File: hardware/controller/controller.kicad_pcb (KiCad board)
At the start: 2 copper layers, 100 x 100 mm, 119 parts, among them J1 230V~, J2 LOAD, J3 DISPLAY, J4 PANEL, J5 TC top, J6 TC bot, J7 USB-C, J9 UART, Q1 AO3401A, Q2 BSS138, Q3 IRLML6346, Q4 IRLML6346, Q5 IRLML6346, Q6 AO3401A, Q7 IRLML6346, SW1 RESET, SW2 BOOT, U1 IRM-10-5, U10 USBLC6-2SC6, U11 USBLC6-2SC6, U12 USBLC6-2SC6, U2 AP7361C-33E, U3 ESP32-S3-WROOM-1U-N8, U4 USBLC6-2SC6, U5 MAX31856MUD+, U6 MAX31856MUD+, U7 SN74LVC74AD, U8 TPS3828-33DBV, U9 TC6501P065

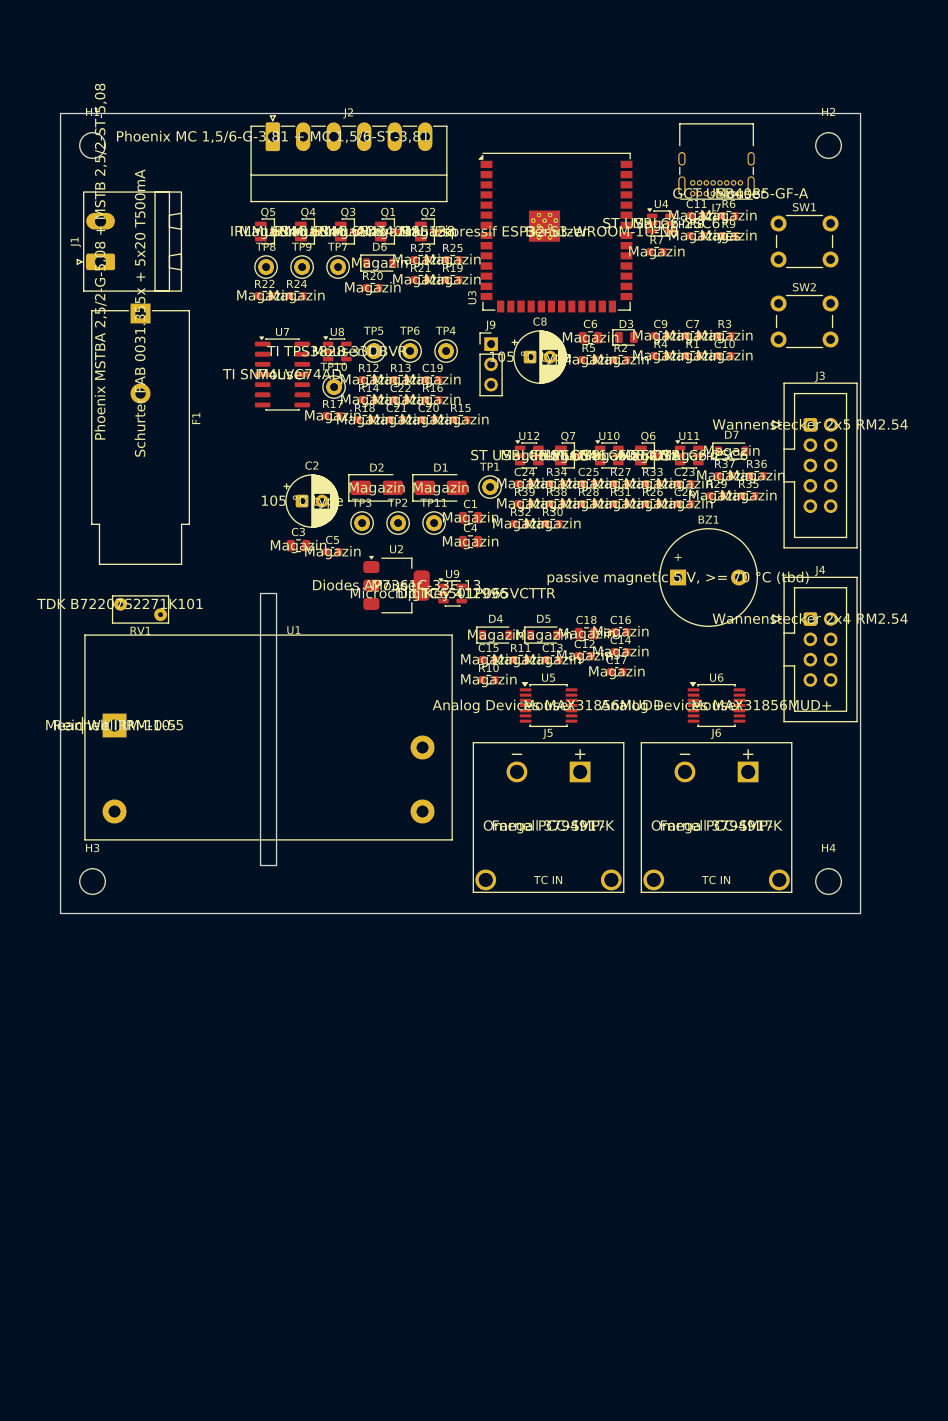
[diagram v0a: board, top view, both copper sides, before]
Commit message: fix(hardware): hide BOM fields on silkscreen, turn J1/J2 to face the board edge
- import_netlist.py sets MPN/Source/DNP fields invisible
- J1 (mains) and J2 (load) rotated 180 deg, plug side flush with the edge
- controller.kicad_pro: defaults added by KiCad 10 on first open

Co-Authored-By: Claude Opus 5.5 <noreply@anthropic.com>
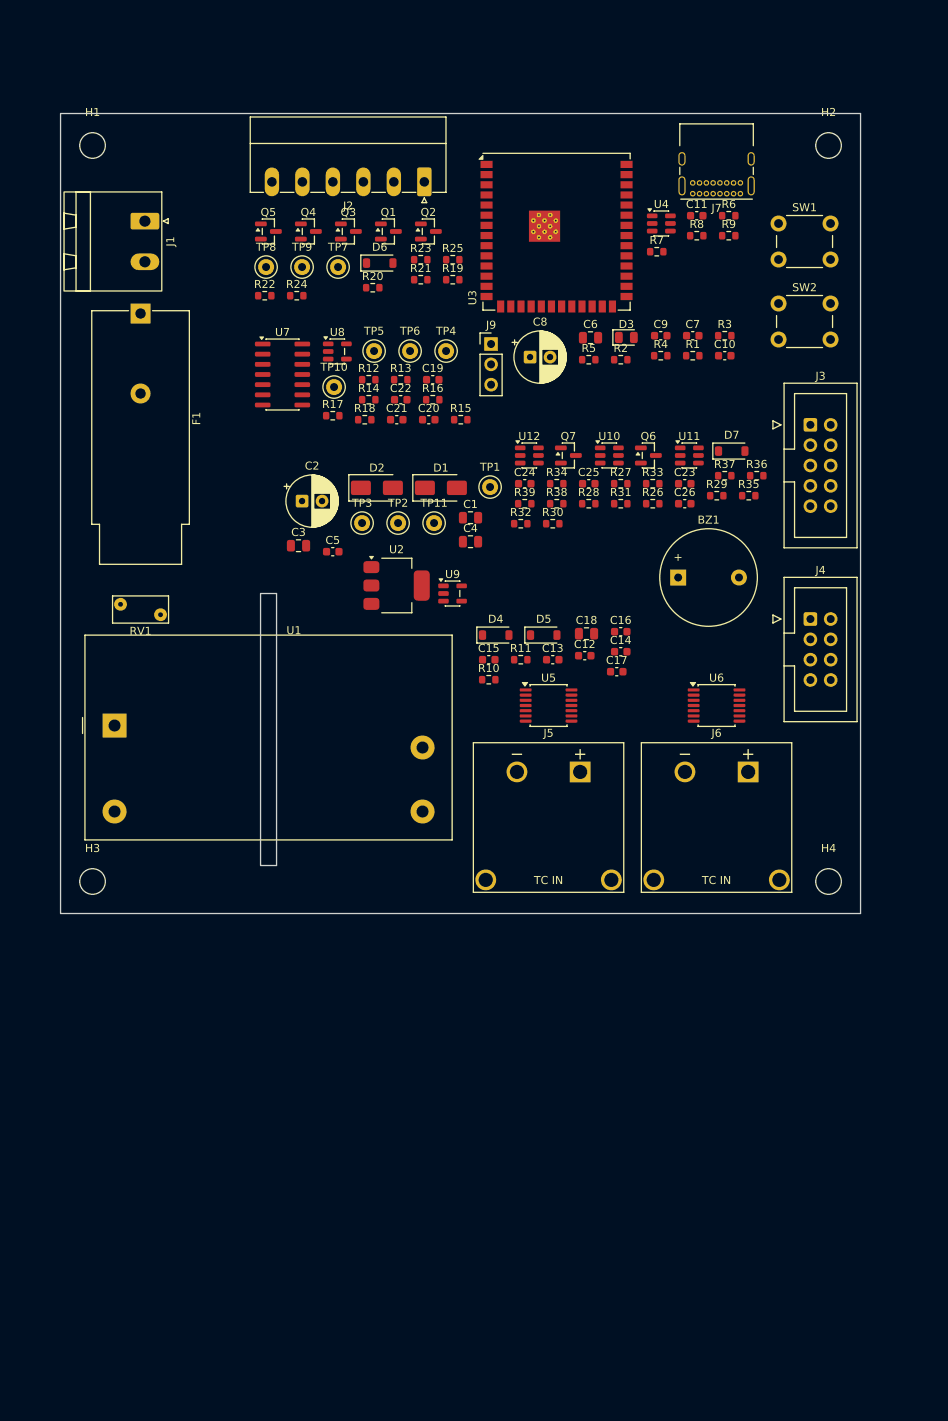
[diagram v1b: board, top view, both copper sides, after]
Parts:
- moved J2 19.8 mm to (45.5, 8.54), turned to 180 degrees
- moved J1 7.53 mm to (10.5, 13.5), turned to -90 degrees

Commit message: feat(hardware): KiCad schematic becomes the source of truth (T071, part 1)
- Schematic template generated once from SKiDL: controller (7 sheets) and encoder carrier
- Verified SKiDL netlists frozen as controller.ref.net / encoder-carrier.ref.net
- tools/check_schematic.py: compares the schematic with the reference (parts,
  connectivity, net names at the ESP32 and of net-class nets) and checks the GPIO
  assignment against board_rev_a.h; 0 errors for both boards
- Generator defects fixed: ENC_B_RAW/ENC_SW_RAW shorted by overlapping wires,
  cp1252 MPN fields, missing labels BOOT, LED_DIAG, L_FUSED (lost net class Mains)
- PCB relinked to the schematic symbols by reference, placement unchanged;
  DRC with --schematic-parity clean; mounting holes board-only
- SKiDL code moved to hardware/archive/skidl; docs and README updated

Co-Authored-By: Claude Opus 5.5 <noreply@anthropic.com>
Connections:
- net FAULT_BOT renamed Net-(D5-K)
- net FAULT_TOP renamed Net-(D4-K)
- net LED_DIAG_A renamed Net-(D3-A)
- net TFT_MOSI renamed Net-(J3-Pin_5)
- net TFT_SCK renamed Net-(J3-Pin_3)
- net USB_CC1 renamed Net-(J7-CC1)
- net USB_CC2 renamed Net-(J7-CC2)
- net USB_SHIELD renamed Net-(J7-SHIELD)
- J7 pad A8: (no net) -> unconnected-(J7-SBU1-PadA8)
- J7 pad B8: (no net) -> unconnected-(J7-SBU2-PadB8)
- U3 pad 15: (no net) -> unconnected-(U3-IO3-Pad15)
- U3 pad 16: (no net) -> unconnected-(U3-IO46-Pad16)
- U3 pad 25: (no net) -> unconnected-(U3-IO48-Pad25)
- U3 pad 26: (no net) -> unconnected-(U3-IO45-Pad26)
- U3 pad 30: (no net) -> unconnected-(U3-IO37-Pad30)
- U3 pad 31: (no net) -> unconnected-(U3-IO38-Pad31)
- U5 pad 6: (no net) -> unconnected-(U5-DNC-Pad6)
- U5 pad 7: (no net) -> unconnected-(U5-~{DRDY}-Pad7)
- U6 pad 6: (no net) -> unconnected-(U6-DNC-Pad6)
- U6 pad 7: (no net) -> unconnected-(U6-~{DRDY}-Pad7)
- U7 pad 6: (no net) -> unconnected-(U7A-~{Q}-Pad6)
- U7 pad 8: (no net) -> unconnected-(U7B-~{Q}-Pad8)
- U7 pad 9: (no net) -> unconnected-(U7B-Q-Pad9)

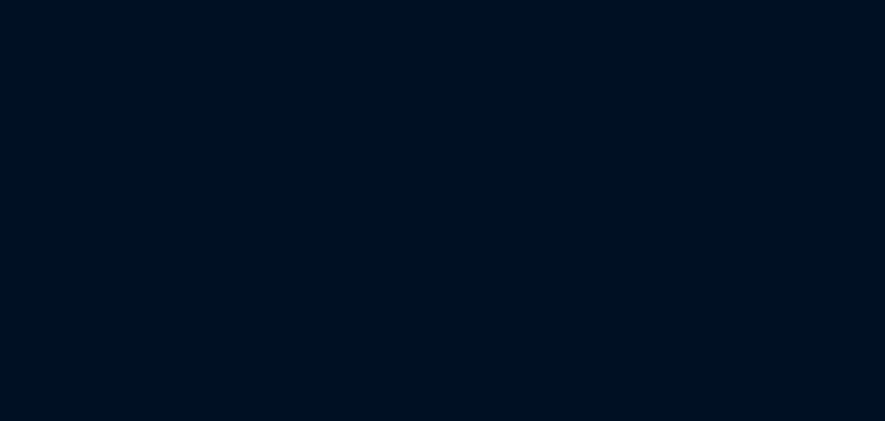
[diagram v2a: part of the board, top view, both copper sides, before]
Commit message: feat(hardware): MAX31856 input filter per datasheet, sheet cleanup in progress
- Input filter per MAX31856 "Typical Application Circuit": C14/C17 100 nF
  differential, new C27-C30 10 nF from T+/T- to GND; reference netlist re-exported
- Datasheet checks: BIAS to T- confirmed, FAULT is push-pull (diodes to CLR needed)
- check_schematic.py: sheet format check (raw newline in strings breaks KiCad)
- import_netlist.py: relinks by reference when a symbol gets a new UUID (U7 case)
- Sheets partly rearranged in KiCad by the user (connectivity unchanged, 0 errors)
- MAX31856 order number and price, docs/Component-Specs ignored

Co-Authored-By: Claude Opus 5.5 <noreply@anthropic.com>
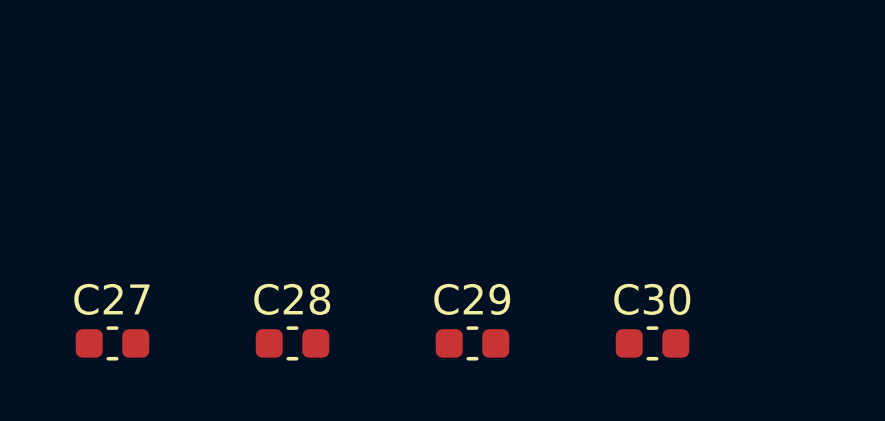
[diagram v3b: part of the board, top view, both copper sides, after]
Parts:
- added C27: 10n, Capacitor_SMD:C_0603_1608Metric, F.Cu at (0.00, 130.0)
- added C28: 10n, Capacitor_SMD:C_0603_1608Metric, F.Cu at (6.00, 130.0)
- added C29: 10n, Capacitor_SMD:C_0603_1608Metric, F.Cu at (12.0, 130.0)
- added C30: 10n, Capacitor_SMD:C_0603_1608Metric, F.Cu at (18.0, 130.0)
- C14, C17: value 10n -> 100n

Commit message: refactor(hardware): merge the 7 controller sheets into 2 (T071)
"Leistung und Sicherheit" (A3: Netzteil, Sicherheit, Last) and
"Steuerung und Messung" (A2: MCU, USB, Thermoelemente, Bedienung).
Contents are only moved, not rewired; each former sheet gets a labelled
frame. check_schematic: 119 parts, 69 nets, 0 errors; ERC unchanged.
PCB relinked by reference, placement unchanged, parity DRC clean.

Co-Authored-By: Claude Opus 5.5 <noreply@anthropic.com>
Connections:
- net ENC_A_RAW renamed /Steuerung und Messung/ENC_A_RAW
- net ENC_B_RAW renamed /Steuerung und Messung/ENC_B_RAW
- net ENC_SW_RAW renamed /Steuerung und Messung/ENC_SW_RAW
- net STOP_NO_RAW renamed /Steuerung und Messung/STOP_NO_RAW
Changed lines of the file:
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@@
 			(layers "F.Cu" "F.Mask" "F.Paste")
 			(roundrect_rratio 0.25)
-			(net "STOP_NO_RAW")
+			(net "/Steuerung und Messung/STOP_NO_RAW")
 		)
 		(pad "2" smd roundrect
@@
 			(layers "F.Cu" "F.Mask" "F.Paste")
 			(roundrect_rratio 0.25)
-			(net "STOP_NO_RAW")
+			(net "/Steuerung und Messung/STOP_NO_RAW")
 		)
 		(embedded_fonts no)
@@
 			(layers "F.Cu" "F.Mask" "F.Paste")
 			(roundrect_rratio 0.25)
-			(net "ENC_SW_RAW")
+			(net "/Steuerung und Messung/ENC_SW_RAW")
 		)
 		(embedded_fonts no)
@@
 			(layers "F.Cu" "F.Mask" "F.Paste")
 			(roundrect_rratio 0.25)
-			(net "ENC_B_RAW")
+			(net "/Steuerung und Messung/ENC_B_RAW")
 		)
 		(pad "2" smd roundrect
@@
 			(layers "F.Cu" "F.Mask" "F.Paste")
 			(roundrect_rratio 0.25)
-			(net "ENC_A_RAW")
+			(net "/Steuerung und Messung/ENC_A_RAW")
 		)
 		(pad "2" smd roundrect
@@
 			(layers "F.Cu" "F.Mask" "F.Paste")
 			(roundrect_rratio 0.25)
-			(net "ENC_B_RAW")
+			(net "/Steuerung und Messung/ENC_B_RAW")
 		)
 		(pad "4" smd roundrect
@@
 			(layers "F.Cu" "F.Mask" "F.Paste")
 			(roundrect_rratio 0.25)
-			(net "ENC_B_RAW")
+			(net "/Steuerung und Messung/ENC_B_RAW")
 		)
 		(pad "5" smd roundrect
@@
 			(layers "F.Cu" "F.Mask" "F.Paste")
 			(roundrect_rratio 0.25)
-			(net "ENC_A_RAW")
+			(net "/Steuerung und Messung/ENC_A_RAW")
 		)
 		(embedded_fonts no)
@@
 			(layers "F.Cu" "F.Mask" "F.Paste")
 			(roundrect_rratio 0.25)
-			(net "ENC_SW_RAW")
+			(net "/Steuerung und Messung/ENC_SW_RAW")
 		)
 		(pad "2" smd roundrect
@@
 			(remove_unused_layers no)
 			(roundrect_rratio 0.147059)
-			(net "ENC_A_RAW")
+			(net "/Steuerung und Messung/ENC_A_RAW")
 		)
 		(pad "2" thru_hole circle
@@
 			(layers "*.Cu" "*.Mask")
 			(remove_unused_layers no)
-			(net "ENC_B_RAW")
+			(net "/Steuerung und Messung/ENC_B_RAW")
 		)
 		(pad "4" thru_hole circle
@@
 			(layers "*.Cu" "*.Mask")
 			(remove_unused_layers no)
-			(net "ENC_SW_RAW")
+			(net "/Steuerung und Messung/ENC_SW_RAW")
 		)
 		(pad "5" thru_hole circle
@@
 			(layers "*.Cu" "*.Mask")
 			(remove_unused_layers no)
-			(net "STOP_NO_RAW")
+			(net "/Steuerung und Messung/STOP_NO_RAW")
 		)
 		(pad "8" thru_hole circle
@@
 			(layers "F.Cu" "F.Mask" "F.Paste")
 			(roundrect_rratio 0.25)
-			(net "ENC_A_RAW")
+			(net "/Steuerung und Messung/ENC_A_RAW")
 		)
 		(pad "2" smd roundrect
@@
 			(layers "F.Cu" "F.Mask" "F.Paste")
 			(roundrect_rratio 0.25)
-			(net "ENC_B_RAW")
+			(net "/Steuerung und Messung/ENC_B_RAW")
 		)
 		(embedded_fonts no)
@@
 			(layers "F.Cu" "F.Mask" "F.Paste")
 			(roundrect_rratio 0.25)
-			(net "ENC_SW_RAW")
+			(net "/Steuerung und Messung/ENC_SW_RAW")
 		)
 		(pad "2" smd roundrect
@@
 			(layers "F.Cu" "F.Mask" "F.Paste")
 			(roundrect_rratio 0.25)
-			(net "STOP_NO_RAW")
+			(net "/Steuerung und Messung/STOP_NO_RAW")
 		)
 		(pad "4" smd roundrect
@@
 			(layers "F.Cu" "F.Mask" "F.Paste")
 			(roundrect_rratio 0.25)
-			(net "STOP_NO_RAW")
+			(net "/Steuerung und Messung/STOP_NO_RAW")
 		)
 		(pad "5" smd roundrect
@@
 			(layers "F.Cu" "F.Mask" "F.Paste")
 			(roundrect_rratio 0.25)
-			(net "ENC_SW_RAW")
+			(net "/Steuerung und Messung/ENC_SW_RAW")
 		)
 		(embedded_fonts no)
@@
 			(layers "F.Cu" "F.Mask" "F.Paste")
 			(roundrect_rratio 0.25)
-			(net "ENC_A_RAW")
+			(net "/Steuerung und Messung/ENC_A_RAW")
 		)
 		(embedded_fonts no)

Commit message: feat(hardware): board fan circuit in the schematic (T073), sheet cleanup in progress
Fan header J10 with BSS138 PWM stage (GPIO 38, 1k pull-up to 5 V,
full speed without firmware) and tachometer input (GPIO 37, 10k/1k/1n,
TP12) per research R18. Reference netlist re-exported for this
deliberate change: 129 parts, 73 nets. board_rev_a.h and
check_schematic.py know FAN_TACH/FAN_PWM. PCB updated from the netlist,
new footprints parked below the outline; parity DRC clean.
Includes the user's partial sheet cleanup (T071 still open).

Co-Authored-By: Claude Opus 5.5 <noreply@anthropic.com>
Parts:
- added C31: 10u, Capacitor_SMD:C_0805_2012Metric, F.Cu at (42.0, 145.0)
- added C32: 100n, Capacitor_SMD:C_0603_1608Metric, F.Cu at (49.0, 145.0)
- added C33: 1n, Capacitor_SMD:C_0603_1608Metric, F.Cu at (56.0, 145.0)
- added J10: FAN, Connector:FanPinHeader_1x04_P2.54mm_Vertical, F.Cu at (0.00, 158.0)
- added Q8: BSS138, Package_TO_SOT_SMD:SOT-23, F.Cu at (7.00, 145.0)
- added R40: 100k, Resistor_SMD:R_0603_1608Metric, F.Cu at (14.0, 145.0)
- added R41: 1k, Resistor_SMD:R_0603_1608Metric, F.Cu at (21.0, 145.0)
- added R42: 10k, Resistor_SMD:R_0603_1608Metric, F.Cu at (28.0, 145.0)
- added R43: 1k, Resistor_SMD:R_0603_1608Metric, F.Cu at (35.0, 145.0)
- added TP12: FAN_TACH, TestPoint:TestPoint_Keystone_5000-5004_Miniature, F.Cu at (63.0, 145.0)
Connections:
- U3 pad 30: unconnected-(U3-IO37-Pad30) -> FAN_TACH
- U3 pad 31: unconnected-(U3-IO38-Pad31) -> FAN_PWM
